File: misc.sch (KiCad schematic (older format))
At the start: 39 parts, among them J13 MICROSD_SLOT_TFP09-2-12B, P13 EXT_SD, P14 LCD, P15 LIMIT_SWITCHES, P16 LIMIT_SWITCHES_V, P17 CONN_01X03, P18 CONN_01X03, P19 CONN_01X03, P20 CONN_01X03, P21 THERMISTORS, P25 I2C, SW1 RESET, U3 ESP-12E

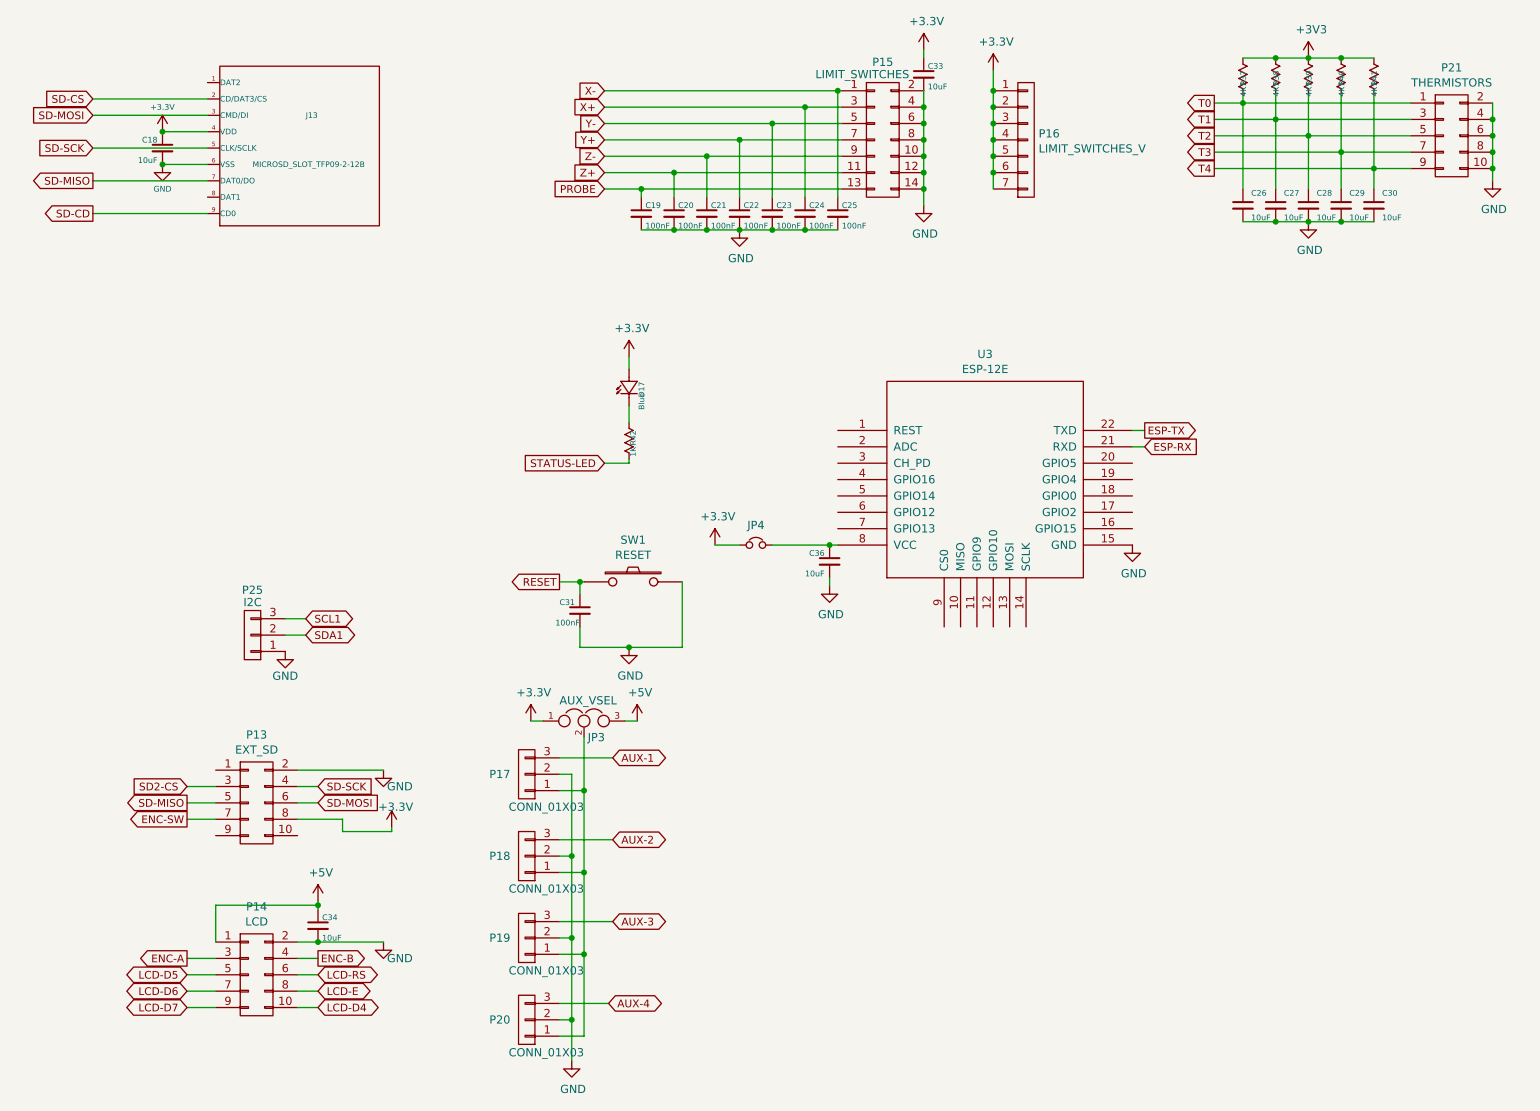
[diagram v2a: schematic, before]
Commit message: Added specifications and manufacturers to component attributes
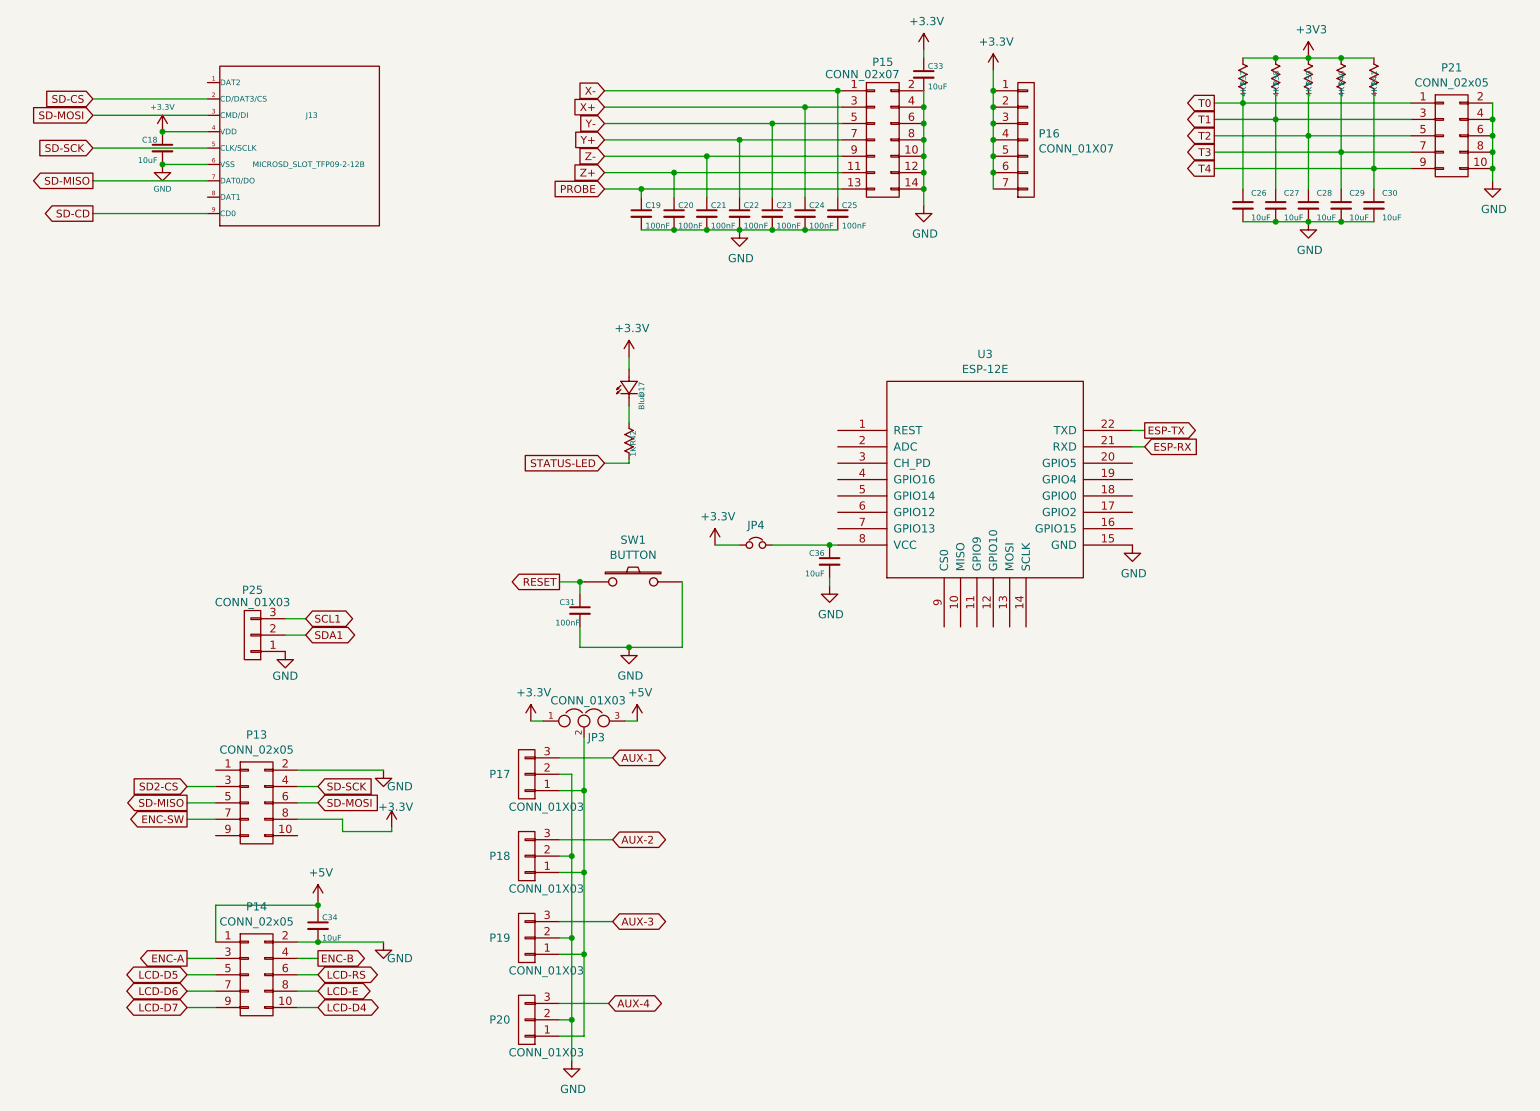
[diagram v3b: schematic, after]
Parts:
- D17: Manufacturer (none) -> Lite-On; ManufacturerNo (none) -> LTST-C193TBKT-5A
- JP3: value AUX_VSEL -> CONN_01X03; Comment (none) -> AUX_VSEL; Specification (none) -> 3 pin 2.54mm pitch single row male header
- JP4: value Jumper_NC_Small -> CONN_01X02; Comment (none) -> Jumper; Specification (none) -> 2 pin 2.54mm pitch single row male header
- P13: value EXT_SD -> CONN_02x05; Comment (none) -> EXT_SD; Specification (none) -> 10 pin 2.54mm pitch dual row male header
- P14: value LCD -> CONN_02x05; Specification (none) -> 10 pin 2.54mm pitch dual row male header
- P15: value LIMIT_SWITCHES -> CONN_02x07; Specification (none) -> 14 pin 2.54mm pitch dual row male header
- P16: value LIMIT_SWITCHES_V -> CONN_01X07; Specification (none) -> 7 pin 2.54mm pitch single row male header
- P17, P18, P19, P20: Specification (none) -> 3 pin 2.54mm pitch single row male header
- P21: value THERMISTORS -> CONN_02x05; Comment (none) -> Thermistors; Specification (none) -> 10 pin 2.54mm pitch dual row male header
- P25: value I2C -> CONN_01X03; Comment (none) -> I2C; Specification (none) -> 3 pin 2.54mm pitch single row male header
- SW1: value RESET -> BUTTON; Manufacturer (none) -> FX; ManufacturerNo (none) -> SMT060606; Specification (none) -> Momentary push button 6x6mm
- U3: description (none) -> ESP8266 WiFi module
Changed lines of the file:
@@
 P 9700 1800
 F 0 "P21" H 9700 2216 50  0000 C CNN
-F 1 "THERMISTORS" H 9700 2124 50  0000 C CNN
+F 1 "CONN_02x05" H 9700 2124 50  0000 C CNN
 F 2 "headers:CON_HDR_2x5_2.54mm" H 9700 600 50  0001 C CNN
 F 3 "" H 9700 600 50  0000 C CNN
+F 4 "Thermistors" H 9700 1800 135 0001 L CNN "Comment"
+F 5 "10 pin 2.54mm pitch dual row male header" H 9700 1800 135 0001 L CNN "Specification"
 	1    9700 1800
 	1    0    0    -1
@@
 P 6225 1825
 F 0 "P15" H 6225 2300 50  0000 C CNN
-F 1 "LIMIT_SWITCHES" H 6100 2225 50  0000 C CNN
+F 1 "CONN_02x07" H 6100 2225 50  0000 C CNN
 F 2 "headers:CON_HDR_2x7_2.54mm" H 6225 625 50  0001 C CNN
 F 3 "" H 6225 625 50  0000 C CNN
+F 4 "14 pin 2.54mm pitch dual row male header" H 6225 1825 135 0001 L CNN "Specification"
 	1    6225 1825
 	1    0    0    -1
@@
 P 7100 1825
 F 0 "P16" H 7177 1863 50  0000 L CNN
-F 1 "LIMIT_SWITCHES_V" H 7177 1771 50  0000 L CNN
+F 1 "CONN_01X07" H 7177 1771 50  0000 L CNN
 F 2 "headers:CON_HDR_1x7_2.54mm" H 7100 1825 50  0001 C CNN
 F 3 "" H 7100 1825 50  0000 C CNN
+F 4 "7 pin 2.54mm pitch single row male header" H 7100 1825 135 0001 L CNN "Specification"
 	1    7100 1825
 	1    0    0    -1
@@
 F 2 "headers:CON_HDR_1x3_2.54mm" H 4050 7200 50  0001 C CNN
 F 3 "" H 4050 7200 50  0000 C CNN
+F 4 "3 pin 2.54mm pitch single row male header" H 4050 7200 135 0001 L CNN "Specification"
 	1    4050 7200
 	-1   0    0    1
@@
 F 2 "headers:CON_HDR_1x3_2.54mm" H 4050 6700 50  0001 C CNN
 F 3 "" H 4050 6700 50  0000 C CNN
+F 4 "3 pin 2.54mm pitch single row male header" H 4050 6700 135 0001 L CNN "Specification"
 	1    4050 6700
 	-1   0    0    1
@@
 F 2 "headers:CON_HDR_1x3_2.54mm" H 4050 6200 50  0001 C CNN
 F 3 "" H 4050 6200 50  0000 C CNN
+F 4 "3 pin 2.54mm pitch single row male header" H 4050 6200 135 0001 L CNN "Specification"
 	1    4050 6200
 	-1   0    0    1
@@
 F 2 "headers:CON_HDR_1x3_2.54mm" H 4050 5700 50  0001 C CNN
 F 3 "" H 4050 5700 50  0000 C CNN
+F 4 "3 pin 2.54mm pitch single row male header" H 4050 5700 135 0001 L CNN "Specification"
 	1    4050 5700
 	-1   0    0    1
@@
 P 2400 5875
 F 0 "P13" H 2400 6291 50  0000 C CNN
-F 1 "EXT_SD" H 2400 6199 50  0000 C CNN
+F 1 "CONN_02x05" H 2400 6199 50  0000 C CNN
 F 2 "headers:CON_HDR_2x5_2.54mm" H 2400 4675 50  0001 C CNN
 F 3 "" H 2400 4675 50  0000 C CNN
+F 4 "EXT_SD" H 2400 5875 135 0001 L CNN "Comment"
+F 5 "10 pin 2.54mm pitch dual row male header" H 2400 5875 135 0001 L CNN "Specification"
 	1    2400 5875
 	1    0    0    -1
@@
 P 2400 6925
 F 0 "P14" H 2400 7341 50  0000 C CNN
-F 1 "LCD" H 2400 7249 50  0000 C CNN
+F 1 "CONN_02x05" H 2400 7249 50  0000 C CNN
 F 2 "headers:CON_HDR_2x5_2.54mm" H 2400 5725 50  0001 C CNN
 F 3 "" H 2400 5725 50  0000 C CNN
+F 4 "10 pin 2.54mm pitch dual row male header" H 2400 6925 135 0001 L CNN "Specification"
 	1    2400 6925
 	1    0    0    -1
@@
 F 2 "diodes:LED-0603" H 4725 3450 60  0001 C CNN
 F 3 "" H 4725 3450 60  0000 C CNN
+F 4 "Lite-On" H 4725 3450 135 0001 L CNN "Manufacturer"
+F 5 "LTST-C193TBKT-5A" H 4725 3450 135 0001 L CNN "ManufacturerNo"
 	1    4725 3450
 	0    -1   -1   0
@@
 P 4700 4525
 F 0 "SW1" H 4700 4781 50  0000 C CNN
-F 1 "RESET" H 4700 4689 50  0000 C CNN
+F 1 "BUTTON" H 4700 4689 50  0000 C CNN
 F 2 "buttons_switches:BUTTON_PUSH_SMD_6x6mm" H 4700 4525 50  0001 C CNN
 F 3 "" H 4700 4525 50  0000 C CNN
+F 4 "FX" H 4700 4525 135 0001 L CNN "Manufacturer"
+F 5 "SMT060606" H 4700 4525 135 0001 L CNN "ManufacturerNo"
+F 6 "Momentary push button 6x6mm" H 4700 4525 135 0001 L CNN "Specification"
 	1    4700 4525
 	1    0    0    -1
@@
 F 4 "AI-Thinker" H 6850 3900 135 0001 L CNN "Manufacturer"
 F 5 "ESP-12E" H 6850 3900 135 0001 L CNN "ManufacturerNo"
+F 6 "ESP8266 WiFi module" H 6850 3900 135 0001 L CNN "description"
 	1    6850 3900
 	1    0    0    -1
@@
 P 2375 4850
 F 0 "P25" H 2375 4575 50  0000 C CNN
-F 1 "I2C" H 2375 4650 50  0000 C CNN
+F 1 "CONN_01X03" H 2375 4650 50  0000 C CNN
 F 2 "headers:CON_HDR_1x3_2.54mm" H 2375 4850 50  0001 C CNN
 F 3 "" H 2375 4850 50  0000 C CNN
+F 4 "I2C" H 2375 4850 135 0001 L CNN "Comment"
+F 5 "3 pin 2.54mm pitch single row male header" H 2375 4850 135 0001 L CNN "Specification"
 	1    2375 4850
 	-1   0    0    1
@@
 P 4400 5375
 F 0 "JP3" H 4475 5275 50  0000 C CNN
-F 1 "AUX_VSEL" H 4425 5500 50  0000 C CNN
+F 1 "CONN_01X03" H 4425 5500 50  0000 C CNN
 F 2 "headers:CON_HDR_1x3_2.54mm" H 4400 5375 50  0001 C CNN
 F 3 "" H 4400 5375 50  0000 C CNN
+F 4 "AUX_VSEL" H 4400 5375 135 0001 L CNN "Comment"
+F 5 "3 pin 2.54mm pitch single row male header" H 4400 5375 135 0001 L CNN "Specification"
 	1    4400 5375
 	1    0    0    -1
@@
 P 5450 4300
 F 0 "JP4" H 5450 4421 50  0000 C CNN
-F 1 "Jumper_NC_Small" H 5460 4240 50  0001 C CNN
+F 1 "CONN_01X02" H 5460 4240 50  0001 C CNN
 F 2 "headers:CON_HDR_1x2_2.54mm" H 5450 4421 50  0001 C CNN
 F 3 "" H 5450 4300 50  0000 C CNN
+F 4 "Jumper" H 5450 4300 135 0001 L CNN "Comment"
+F 5 "2 pin 2.54mm pitch single row male header" H 5450 4300 135 0001 L CNN "Specification"
 	1    5450 4300
 	1    0    0    -1

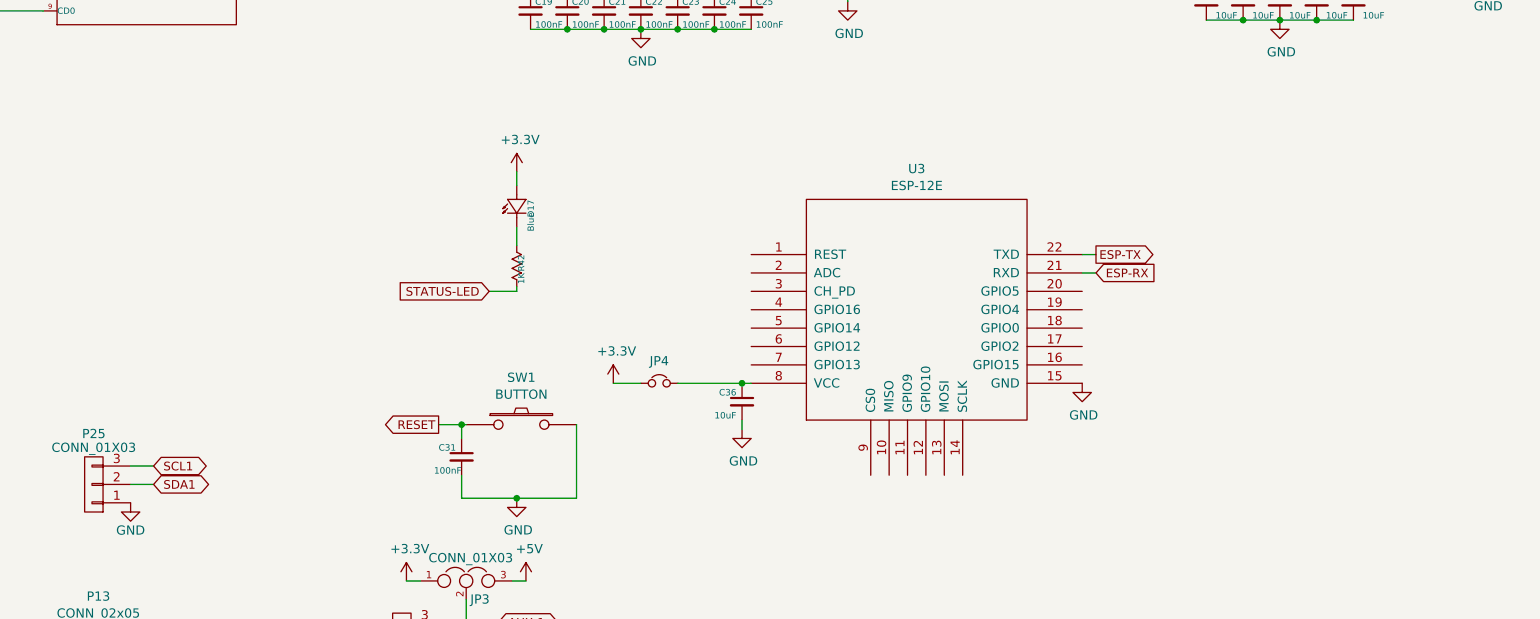
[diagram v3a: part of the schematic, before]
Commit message: fix analog and wifi
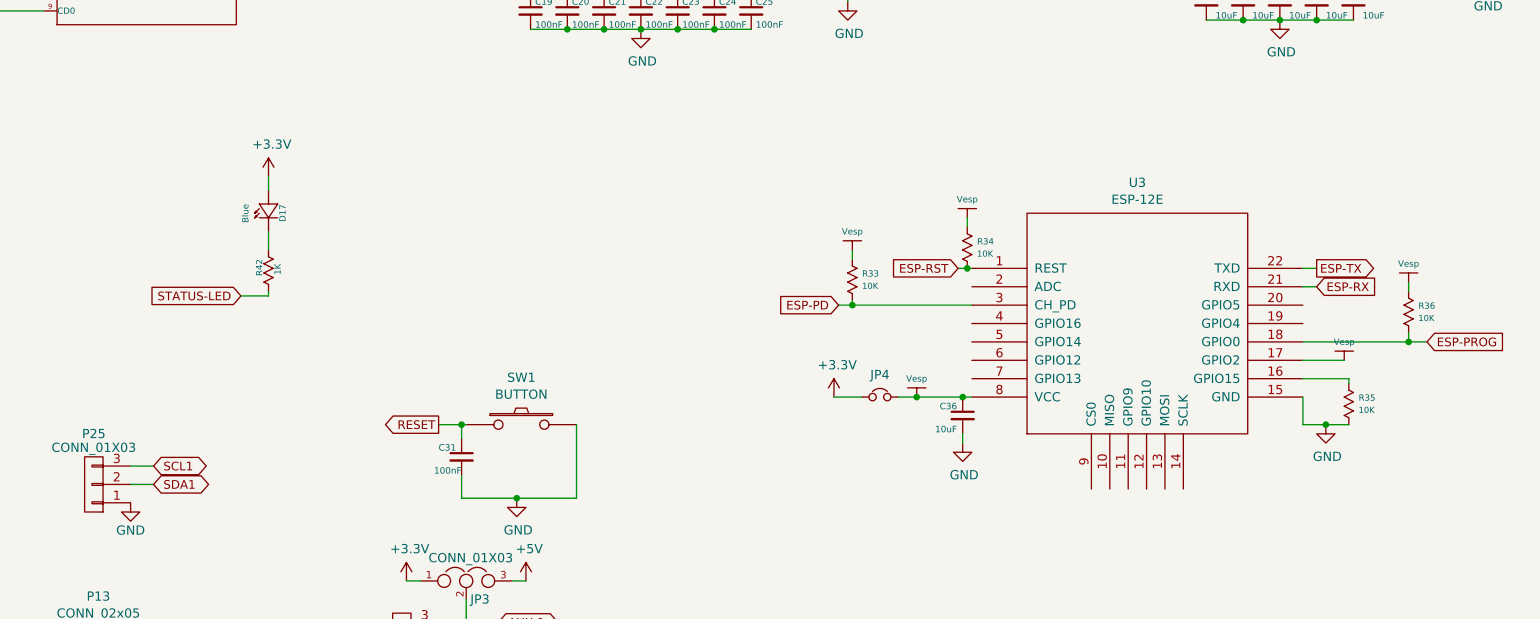
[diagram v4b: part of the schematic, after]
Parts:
- added R33, R34, R35, R36: 10K, resistors:R_0603, symbol RESISTOR
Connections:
- net GND: now also R35.2
- net ESP-RST: now reaches U3.1 (REST)
- net ESP-RST: now also R34.2
- net at U3.16 (GPIO15): now also R35.1
- net Vesp: now reaches U3.17 (GPIO2)
- net Vesp: now also C36.1, JP4.2, U3.8 (VCC), R33.1, R34.1, R36.1
- net ESP-PROG: now reaches U3.18 (GPIO0)
- net ESP-PROG: now also R36.2
- net ESP-PD: now reaches U3.3 (CH_PD)
- net ESP-PD: now also R33.2
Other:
- moved on the sheet: C36, D17, JP4, R42, U3
